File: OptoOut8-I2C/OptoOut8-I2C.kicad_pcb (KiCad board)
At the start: 2 copper layers, 95 x 95 mm, 31 parts, among them J2 DB25, P1 CONN_4, P2 CONN_3X2, P3 CONN_4, U1 4N26, U2 4N26, U3 4N26, U4 4N26, U5 4N26, U6 4N26, U7 4N26, U8 4N26, U9 MCP23008P

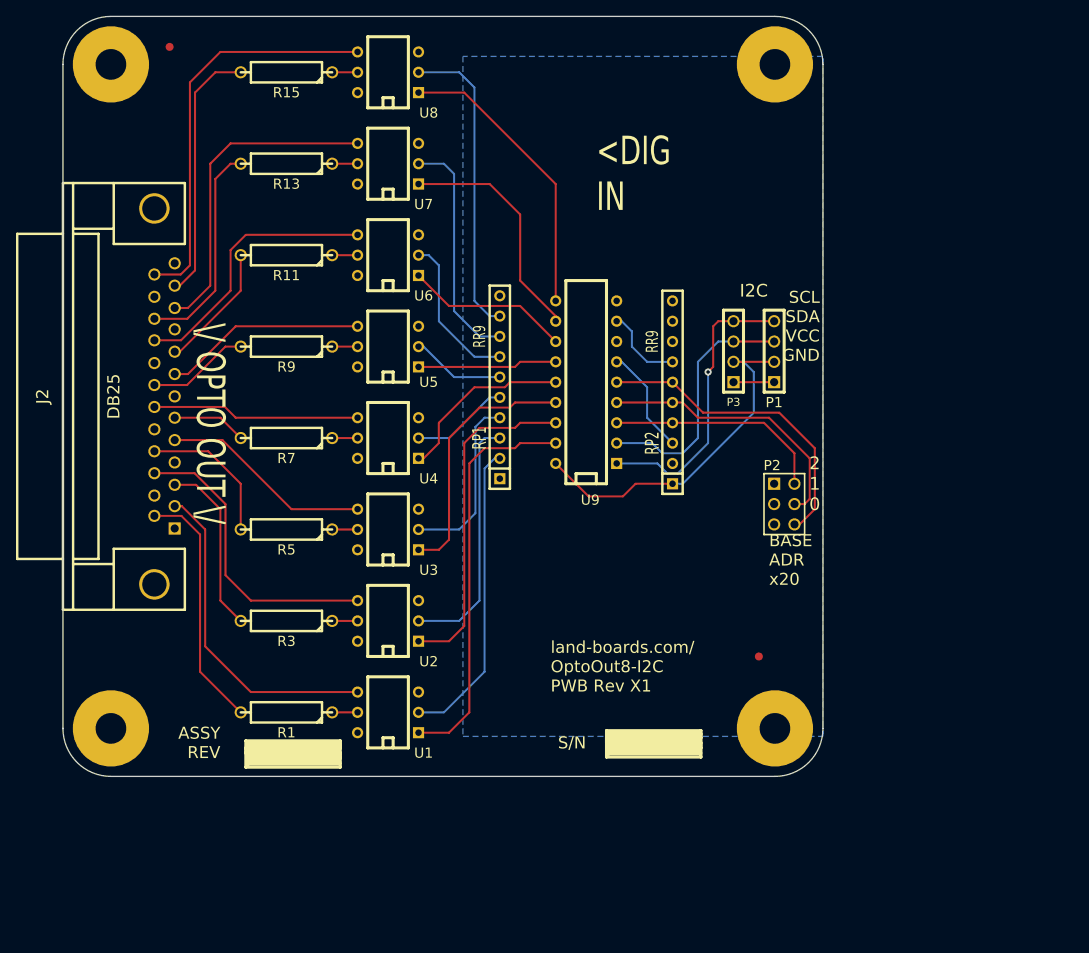
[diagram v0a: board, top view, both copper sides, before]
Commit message: Updates to opto processor
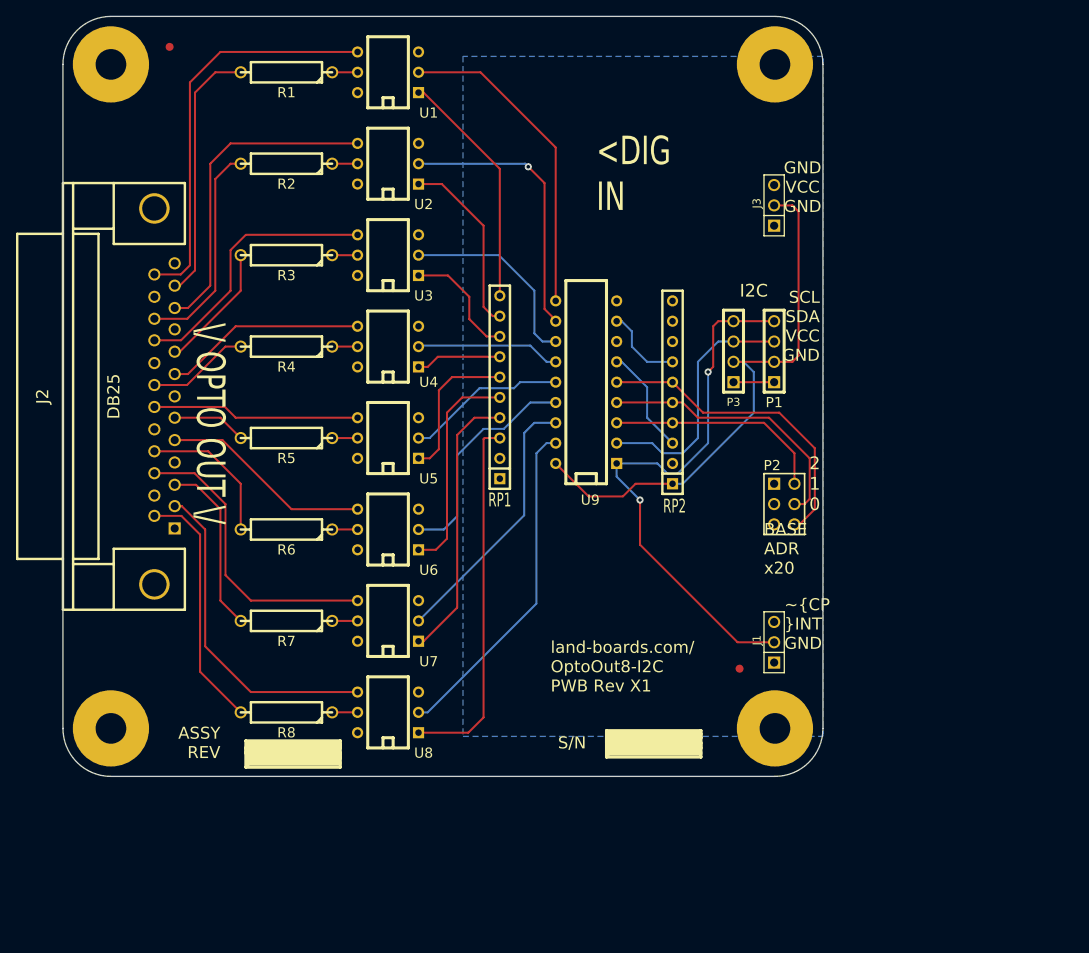
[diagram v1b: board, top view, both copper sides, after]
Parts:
- added J1: CONN_3, PIN_ARRAY_3X1, F.Cu at (88.9, 78.2)
- added J3: CONN_3, PIN_ARRAY_3X1, F.Cu at (88.9, 23.6)
- moved FID1 2.85 mm to (84.6, 81.5)
- renumbered R15 to R1, R13 to R2, R11 to R3, R9 to R4, R7 to R5, R5 to R6, R3 to R7, R1 to R8, ST1 to ST2, U8 to U1, U7 to U2, U6 to U3, U5 to U4, U4 to U5, U3 to U6, U2 to U7, U1 to U8
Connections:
- P1 pad 1: /GND -> GND
- P2 pad 1: /GND -> GND
- P2 pad 3: /GND -> GND
- P2 pad 5: /GND -> GND
- P3 pad 1: /GND -> GND
- RP1 pad 1: /GND -> (no net)
- RP1 pad 10: (no net) -> N-0000043
- RP1 pad 2: N-0000059 (its old number) -> (no net)
- RP1 pad 3: N-0000028 -> N-000009
- RP1 pad 4: N-0000029 -> N-000008
- RP1 pad 5: N-0000027 -> N-000007
- RP1 pad 6: N-0000030 -> N-000006
- RP1 pad 7: N-0000031 -> N-0000046
- RP1 pad 8: N-0000021 -> N-0000045
- RP1 pad 9: N-0000041 -> N-0000044
- U1 pad 1: N-0000011 -> N-0000043
- U1 pad 2: N-0000041 -> N-0000047
- U2 pad 1: N-0000010 -> N-0000044
- U2 pad 2: N-0000021 -> N-0000048
- U3 pad 1: N-0000072 -> N-0000045
- U3 pad 2: N-0000031 -> N-0000049
- U4 pad 1: N-000009 -> N-0000046
- U4 pad 2: N-0000030 -> N-0000040
- U5 pad 1: N-000008 -> N-000006
- U5 pad 2: N-0000027 -> N-0000041
- U6 pad 1: N-0000070 (its old number) -> N-000007
- U6 pad 2: N-0000029 -> N-0000042
- U7 pad 1: N-0000055 (its old number) -> N-000008
- U7 pad 2: N-0000028 -> N-0000039
- U8 pad 1: N-0000068 (its old number) -> N-000009
- U8 pad 2: N-0000059 (its old number) -> N-0000010
- U9 pad 10: N-0000011 -> N-0000047
- U9 pad 11: N-0000010 -> N-0000048
- U9 pad 12: N-0000072 -> N-0000049
- U9 pad 13: N-000009 -> N-0000040
- U9 pad 14: N-000008 -> N-0000041
- U9 pad 15: N-0000070 (its old number) -> N-0000042
- U9 pad 16: N-0000055 (its old number) -> N-0000039
- U9 pad 17: N-0000068 (its old number) -> N-0000010
- U9 pad 9: /GND -> GND
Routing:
- net N-0000068 (its old number): track 50.4 -> 0.00 mm
- net N-0000055 (its old number): track 41.8 -> 0.00 mm
- net N-0000047: track 0.00 -> 40.2 mm
- net N-0000059 (its old number): track 38.2 -> 0.00 mm
- net N-0000011: track 36.5 -> 0.00 mm
- net N-0000048: track 0.00 -> 34.6 mm, vias 0 -> 1
- net N-0000039: track 0.00 -> 33.4 mm
- net /SCL: track 36.3 -> 69.5 mm, vias 1 -> 2
- net N-0000070 (its old number): track 32.2 -> 0.00 mm
- net N-0000028: track 31.2 -> 0.00 mm
- net N-0000043: track 0.00 -> 30.0 mm
- net N-0000021: track 29.1 -> 0.00 mm
- net N-000009: track 17.4 -> 45.8 mm
- net N-0000042: track 0.00 -> 28.2 mm
- net N-000007: track 0.00 -> 27.3 mm
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- added copper zone on B.Cu, net GND
- removed copper zone on B.Cu, net /GND
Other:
- board text added: "GND VCC GND"
- board text added: "~CP ~INT GND"

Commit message: Tweeks to optos
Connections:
- J1 pad 2: /SCL -> (no net)
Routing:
- net /SCL: track 69.5 -> 36.3 mm, vias 2 -> 1

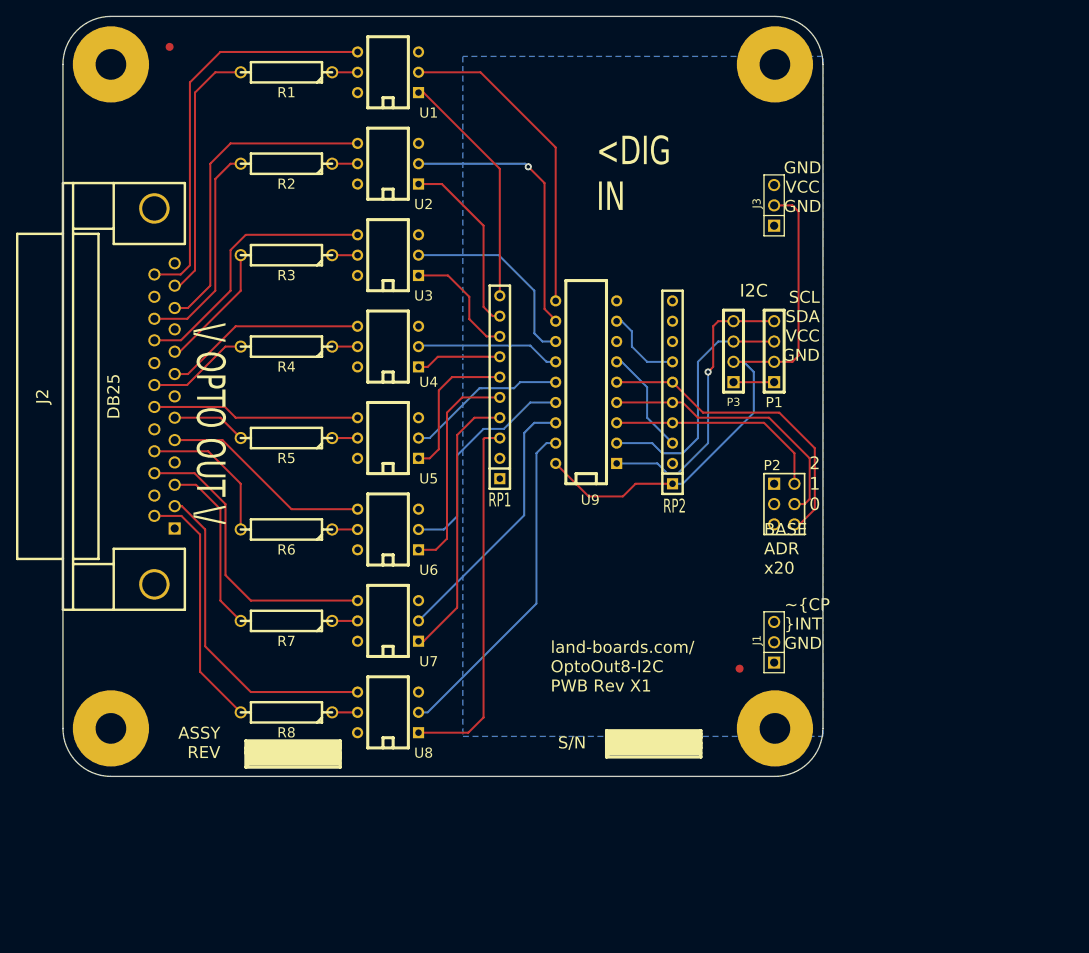
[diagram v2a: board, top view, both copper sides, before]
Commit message: lined up connectors
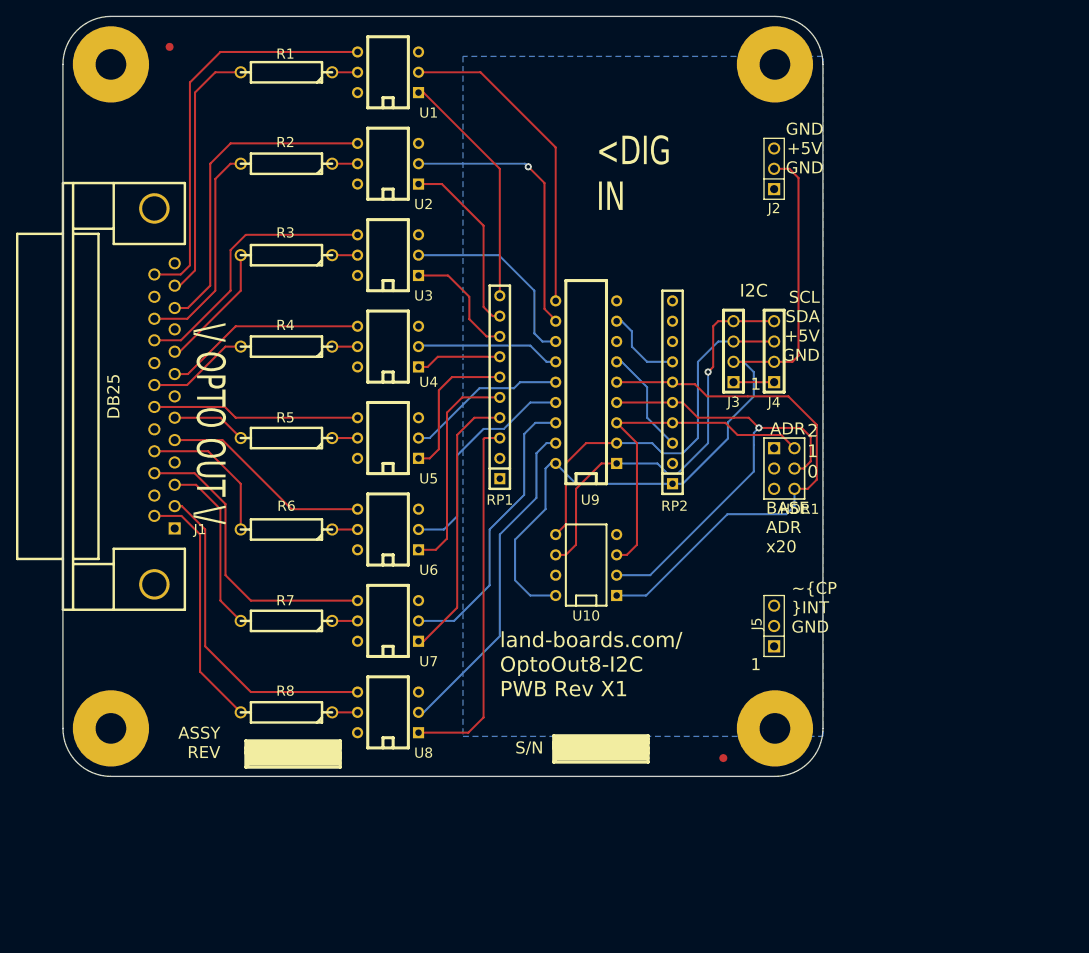
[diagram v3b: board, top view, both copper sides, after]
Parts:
- removed P2: CONN_3X2, pin_array_3x2
- added HDR1: CONN_3X2, pin_array_3x2, F.Cu at (90.2, 56.5)
- added U10: 24C01, DIP-8__300, F.Cu at (65.4, 68.6)
- moved FID1 10.9 mm to (80.0, 91.4)
- moved ST1 6.63 mm to (67.7, 91.4)
- moved J2 4.57 mm to (88.9, 19.1)
- moved J5 2.03 mm to (88.9, 76.2)
- renumbered J2 to J1, J3 to J2, P3 to J3, P1 to J4, J1 to J5
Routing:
- net /A0: track 39.1 -> 66.4 mm
- net /VCC: track 68.8 -> 94.8 mm
- net /A1: track 34.3 -> 59.7 mm, vias 0 -> 1
- net /SDA: track 31.6 -> 48.4 mm
- net /SCL: track 36.3 -> 52.7 mm
- net /A2: track 27.6 -> 42.9 mm
- net N-000008: track 33.4 -> 36.0 mm
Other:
- board text added: "1"
- board text added: "ADR"
- board text added: "GND +5V GND"
- board text added: "SCL SDA +5V GND"
- board text removed: "GND VCC GND"
- board text removed: "SCL SDA VCC GND"

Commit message: docs
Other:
- board text added: "land-boards.com/ OptoOut8-I2C PWB Rev X2"
- board text removed: "land-boards.com/ OptoOut8-I2C PWB Rev X1"
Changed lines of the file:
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@@
-(kicad_pcb (version 3) (host pcbnew "(2013-05-31 BZR 4019)-stable")
+(kicad_pcb (version 3) (host pcbnew "(2013-04-19 BZR 4011)-stable")
   (general
     (links 72)
@@
       (usegerberextensions true)
       (excludeedgelayer true)
-      (linewidth 0.150000)
+      (linewidth 0)
       (plotframeref false)
       (viasonmask false)
@@
     (descr "Connecteur 3 pins")
     (tags "CONN DEV")
-    (fp_text reference J5 (at 0.254 -2.159 90) (layer F.SilkS)
+    (fp_text reference J5 (at -4.9 -0.2 180) (layer F.SilkS)
       (effects (font (size 1.27 1.27) (thickness 0.3175)))
     )
@@
     )
   )
-  (gr_text "land-boards.com/\nOptoOut8-I2C\nPWB Rev X1" (at 80 81) (layer B.SilkS)
+  (gr_text "land-boards.com/\nOptoOut8-I2C\nPWB Rev X2" (at 80 81) (layer B.SilkS)
     (effects (font (size 1.905 1.905) (thickness 0.381)) (justify left mirror))
   )
@@
     (effects (font (size 1.5 1.5) (thickness 0.3)) (justify left))
   )
-  (gr_text 1 (at 86.614 81.026) (layer F.SilkS)
+  (gr_text 1 (at 86.7 79) (layer F.SilkS)
     (effects (font (size 1.5 1.5) (thickness 0.3)))
   )
@@
     (effects (font (size 1.5 1.5) (thickness 0.3)))
   )
-  (gr_text "GND\n+5V\nGND" (at 92.71 16.51) (layer F.SilkS)
+  (gr_text "GND\n+5V\nGND" (at 92.5 16.8) (layer F.SilkS)
     (effects (font (size 1.5 1.5) (thickness 0.3)))
   )
-  (gr_text "~CP\n~INT\nGND" (at 91.059 73.914) (layer F.SilkS)
+  (gr_text "~CP\n~INT\nGND" (at 90.2 74.1) (layer F.SilkS)
     (effects (font (size 1.5 1.5) (thickness 0.3)) (justify left))
   )
@@
     (effects (font (size 1.5 1.5) (thickness 0.3)) (justify left))
   )
-  (gr_text "land-boards.com/\nOptoOut8-I2C\nPWB Rev X1" (at 54.61 81.026) (layer F.SilkS)
+  (gr_text "land-boards.com/\nOptoOut8-I2C\nPWB Rev X2" (at 54.61 81.026) (layer F.SilkS)
     (effects (font (size 1.905 1.905) (thickness 0.381)) (justify left))
   )

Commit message: rev x2
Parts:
- added J5: CONN_02X02, Pin_Headers:Pin_Header_Straight_2x02, F.Cu at (91.2, 68.1)
- added R10: R, Discret:R4-5, F.Cu at (78.7, 76.8)
- added R9: R, Discret:R4-5, F.Cu at (81.5, 76.9)
- renumbered J2 to J1, J3 to J2, J4 to J3, HDR1 to J4, J5 to J6, J1 to J7
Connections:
- net N-0000051 renamed /OPTO0-PLUS
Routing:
- net /VCC: track 94.8 -> 124.2 mm, vias 0 -> 3
- net /SDA: track 48.4 -> 72.1 mm, vias 0 -> 1
- net /SCL: track 52.7 -> 75.4 mm, vias 1 -> 3
- net Net-(J5-Pad3): track 0.00 -> 15.7 mm
- net Net-(J5-Pad1): track 0.00 -> 12.0 mm
- net /A1: track 59.7 -> 58.8 mm
- net Net-(J7-Pad22): track 33.8 -> 34.5 mm
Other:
- net class Default: clearance 0.254 -> 0.2032
- rule trace_clearance: 0.254 -> 0.2032
- board text added: "D C"
- board text added: "GND +V GND"
- board text added: "I2C TERM"
- board text added: "PWB Rev X2"
- board text added: "SCL SDA +V GND"
- board text added: "land-boards.com/ OptoOut8-I2C"
- board text removed: "<DIG IN"
- board text removed: "GND +5V GND"
- board text removed: "SCL SDA +5V GND"
- board text removed: "land-boards.com/ OptoOut8-I2C PWB Rev X2"

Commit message: Working on ODAS layouts
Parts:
- added R9: 1K, Discret:R4-5, F.Cu at (76.2, 76.7)
- J4: footprint pin_array_3x2 -> Pin_Headers:Pin_Header_Straight_2x03
- J5: value CONN_02X02 -> CONN_02X03; footprint Pin_Headers:Pin_Header_Straight_2x02 -> Pin_Headers:Pin_Header_Straight_2x03
- R10: value R -> 2.2K
- R11: renamed from R9; value R -> 2.2K
- RP2: value RR9 -> 4.7K
- moved J4 2.53 mm to (90.9, 58.9), turned to 180 degrees
- moved J5 0.95 mm to (91.2, 69.1)
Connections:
- J5 pad 1: Net-(J5-Pad1) -> GND
- J5 pad 2: /SCL -> Net-(J5-Pad2)
- J5 pad 4: /SDA -> /SCL
- R10 pad 1: Net-(J5-Pad3) -> Net-(J5-Pad5)
- R11 pad 1: Net-(J5-Pad1) -> Net-(J5-Pad3)
- U10 pad 7: (no net) -> Net-(J5-Pad2)
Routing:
- net Net-(J5-Pad2): track 0.00 -> 34.0 mm
- net Net-(RP1-Pad10): track 30.0 -> 60.7 mm
- net Net-(J5-Pad5): track 0.00 -> 19.8 mm, vias 0 -> 1
- net Net-(J5-Pad1): track 12.0 -> 0.00 mm
- net /SDA: track 72.1 -> 79.8 mm
- net /SCL: track 75.4 -> 82.1 mm, vias 3 -> 2
- net /A1: track 58.8 -> 52.8 mm, vias 1 -> 3
- net /A0: track 66.0 -> 60.5 mm, vias 0 -> 1
- net GND: track 5.08 -> 0.00 mm
- net Net-(J5-Pad3): track 15.7 -> 12.3 mm
- net /A2: track 42.9 -> 45.4 mm, vias 0 -> 2
- net /VCC: track 124.2 -> 125.9 mm, vias 3 -> 2
- net Net-(RP1-Pad8): track 15.0 -> 13.3 mm
- net Net-(RP1-Pad5): track 27.3 -> 25.6 mm
- net Net-(RP1-Pad6): track 18.7 -> 17.6 mm
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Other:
- board text added: "BASE ADR x50"
- board text added: "I2C| TERM| WEN"
- board text added: "POWER"
- board text removed: "I2C TERM"

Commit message: X2 boards - as ordered
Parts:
- added C1: C, Capacitors_ThroughHole:C_Rect_L7_W2_P5, F.Cu at (93.0, 80.3)
- added C2: C, Capacitors_ThroughHole:C_Rect_L7_W2_P5, F.Cu at (93.0, 97.8)
- added TESTED: VAL**, modules:TEST_BLK-REAR, F.Cu at (36.6, 100.3)
- U10: footprint DIP-8__300 -> Housings_DIP:DIP-8__300_ELL
- U9: footprint DIP-18__300 -> Housings_DIP:DIP-18__300_ELL
- moved J7 36.1 mm to (42.7, 67.5)
- moved FID1 36.1 mm to (110.0, 111.4)
- moved FID2 36.1 mm to (43.3, 23.8)
- moved J2 36.1 mm to (113.8, 65.7)
- moved J3 36.1 mm to (118.9, 65.7)
- moved J4 36.1 mm to (120.9, 78.9)
- moved J5 36.1 mm to (121.2, 89.1)
- moved J6 36.1 mm to (118.9, 96.2)
- moved MTG1 36.1 mm to (119.0, 109.0)
- moved MTG2 36.1 mm to (36.0, 109.0)
- moved MTG3 36.1 mm to (119.0, 26.0)
- moved MTG4 36.1 mm to (36.0, 26.0)
- moved R1 36.1 mm to (57.9, 27.0)
- moved R10 36.1 mm to (108.7, 96.8)
- moved R11 36.1 mm to (111.5, 96.9)
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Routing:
- net /VCC: track 125.9 -> 166.6 mm, vias 2 -> 3
- net /A0: track 60.5 -> 55.6 mm
- net /SDA: track 79.8 -> 76.1 mm, vias 1 -> 2
- net Net-(U8-Pad2): track 41.8 -> 43.6 mm
- net /A1: track 52.8 -> 51.4 mm
- net /A2: track 45.4 -> 46.2 mm
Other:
- net class POWER added: clearance 0.635, trace_width 0.635, via_dia 0.889, via_drill 0.635
- board text added: "A0 A1 A2"
- board text added: "I2C TERM WEN"
- board text removed: "2 1 0"
- board text removed: "I2C| TERM| WEN"
